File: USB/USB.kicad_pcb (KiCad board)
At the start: 4 copper layers, 36.9 x 37.9 mm, 41 parts, among them J1 MISC1, U1 TLV61222

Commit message: Update
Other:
- board text added: "PCB3D_BR_USB"
- board text added: "PCB3D_TL_USB"

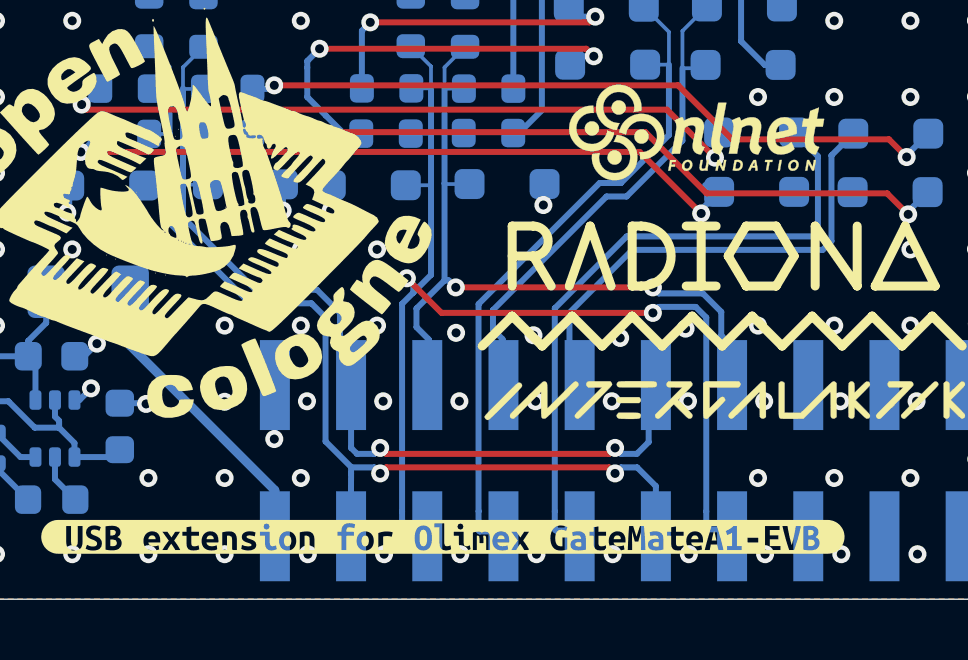
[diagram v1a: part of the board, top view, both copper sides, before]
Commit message: Updating USB
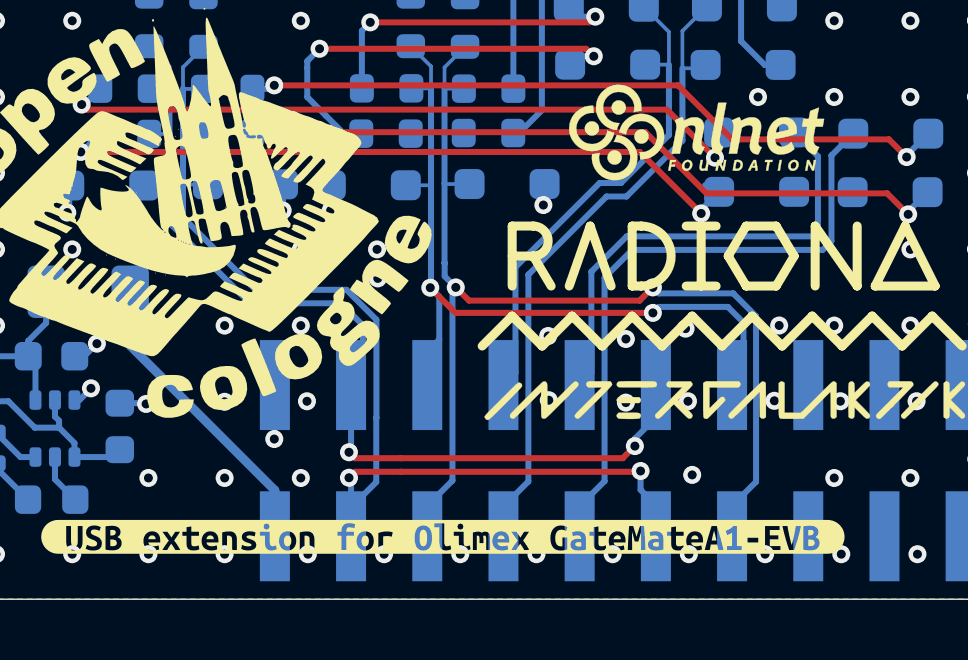
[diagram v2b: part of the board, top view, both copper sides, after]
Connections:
- J1 pad 10: USB1_FPGA_PULL_D+ -> USB1_FPGA_PULL_D-
- J1 pad 11: USB1_FPGA_D- -> USB1_FPGA_D+
- J1 pad 12: USB1_FPGA_D+ -> USB1_FPGA_D-
- J1 pad 13: USB2_FPGA_D- -> USB2_FPGA_D+
- J1 pad 14: USB2_FPGA_D+ -> USB2_FPGA_D-
- J1 pad 15: GN00 -> GP00
- J1 pad 16: GP00 -> GN00
- J1 pad 17: GN01 -> GP01
- J1 pad 18: GP01 -> GN01
- J1 pad 19: GN02 -> GP02
- J1 pad 20: GP02 -> GN02
- J1 pad 3: USB1_FPGA_D- -> USB1_FPGA_D+
- J1 pad 4: USB1_FPGA_D+ -> USB1_FPGA_D-
- J1 pad 5: USB2_FPGA_D- -> USB2_FPGA_D+
- J1 pad 6: USB2_FPGA_D+ -> USB2_FPGA_D-
- J1 pad 7: USB2_FPGA_PULL_D- -> USB2_FPGA_PULL_D+
- J1 pad 8: USB2_FPGA_PULL_D+ -> USB2_FPGA_PULL_D-
- J1 pad 9: USB1_FPGA_PULL_D- -> USB1_FPGA_PULL_D+
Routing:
- net USB2_FPGA_D-: track 39.1 -> 27.4 mm
- net USB2_FPGA_D+: track 26.5 -> 37.7 mm
- net USB2_FPGA_PULL_D-: track 22.5 -> 16.5 mm
- net USB1_FPGA_PULL_D-: track 22.6 -> 16.6 mm
- net USB1_FPGA_D+: track 31.8 -> 37.8 mm
- net USB1_FPGA_PULL_D+: track 16.9 -> 21.7 mm
- net USB2_FPGA_PULL_D+: track 16.9 -> 21.7 mm
- net USB1_FPGA_D-: track 35.0 -> 34.0 mm
- net GND: vias 151 -> 148

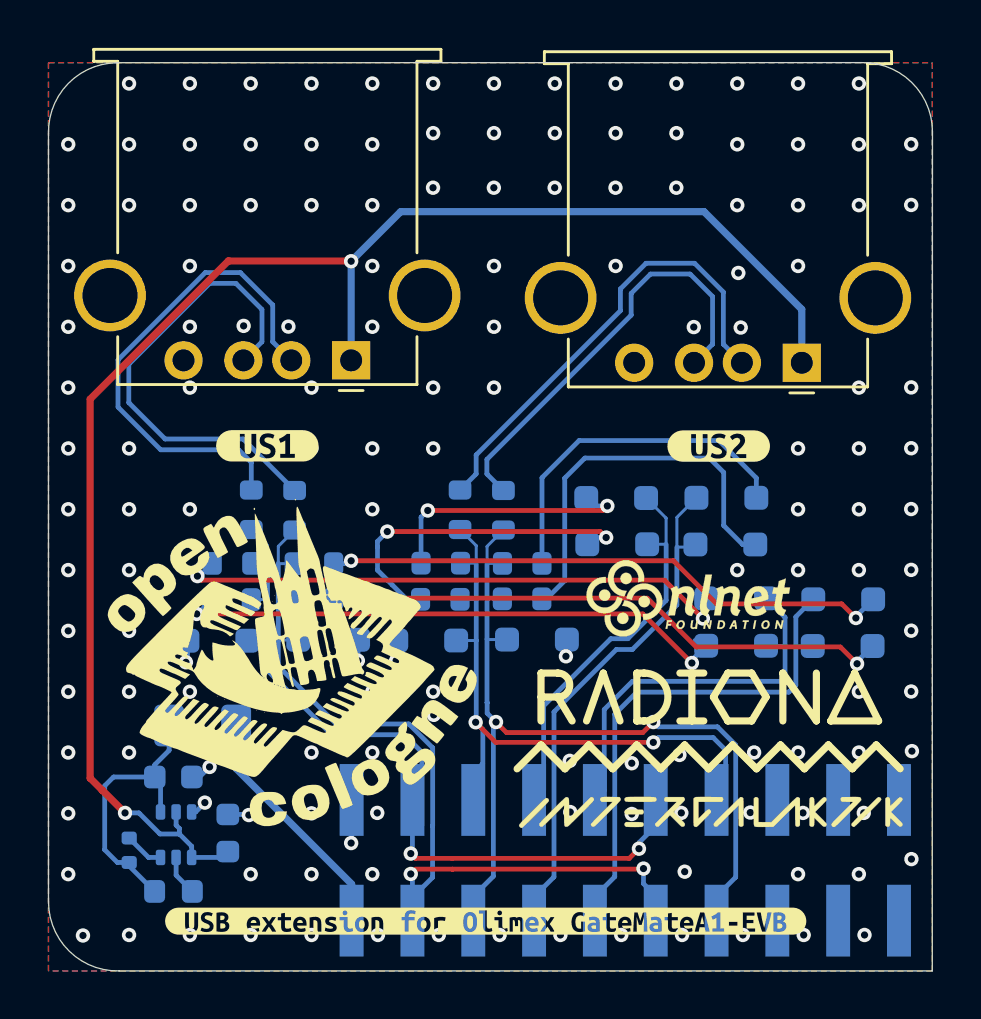
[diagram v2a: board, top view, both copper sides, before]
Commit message: Adding voltage level converter for USB
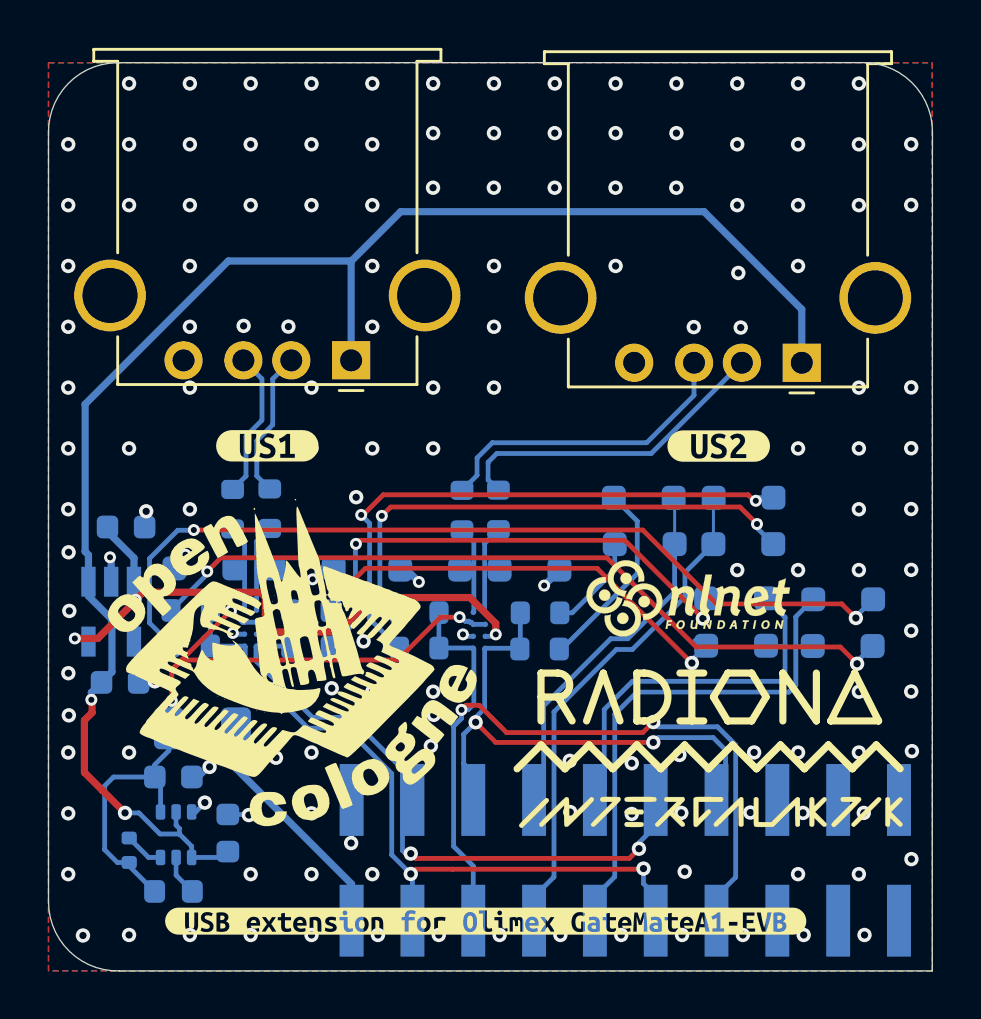
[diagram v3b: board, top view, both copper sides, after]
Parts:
- added C3: 1u, Capacitor_SMD:C_0603_1608Metric, B.Cu at (87.1, 110.0)
- added C4: 1u, Capacitor_SMD:C_0603_1608Metric, B.Cu at (87.3, 103.5)
- added IC1: TXS0202YZPR, TXS0202YZPR:BGA8C50P2X4_89X189X50, B.Cu at (92.5, 107.7)
- added IC2: NCV8730ASN330T1G, NCV8730ASN330T1G:SOT95P275X110-5N, B.Cu at (86.7, 107.0)
- added IC3: TXS0202YZPR, TXS0202YZPR:BGA8C50P2X4_89X189X50, B.Cu at (102.1, 107.8)
- moved R2 6.19 mm to (90.0, 108.4), turned to 0 degrees
- moved D5 5.97 mm to (90.6, 105.2), turned to 180 degrees
- moved R8 5.57 mm to (99.6, 108.5), turned to 0 degrees
- moved R10 5.47 mm to (104.6, 108.6), turned to 180 degrees
- moved D12 5.33 mm to (100.0, 105.3), turned to 180 degrees
- moved D14 5.23 mm to (104.2, 105.3), turned to 0 degrees
- moved R1 5.16 mm to (90.0, 107.0), turned to 0 degrees
- moved R4 4.79 mm to (95.0, 108.5), turned to 180 degrees
- moved D7 4.70 mm to (94.7, 105.2), turned to 0 degrees
- moved R7 4.33 mm to (99.6, 107.1), turned to 0 degrees
- moved R9 4.20 mm to (104.6, 107.1), turned to 0 degrees
- moved R3 3.33 mm to (95.0, 107.0), turned to 0 degrees
- moved R6 2.59 mm to (91.8, 102.7)
- moved R12 1.73 mm to (101.3, 102.8)
- moved R11 1.60 mm to (102.9, 102.8)
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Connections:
- D12 pad 1: USB2_FPGA_D+ -> /USB2_DEVICE_D+
- D14 pad 1: USB2_FPGA_D- -> /USB2_DEVICE_D-
- D5 pad 1: USB1_FPGA_D+ -> /USB1_DEVICE_D+
- D7 pad 1: USB1_FPGA_D- -> /USB1_DEVICE_D-
- R11 pad 1: USB2_FPGA_D- -> /USB2_DEVICE_D-
- R12 pad 1: USB2_FPGA_D+ -> /USB2_DEVICE_D+
- R5 pad 1: USB1_FPGA_D- -> /USB1_DEVICE_D-
- R6 pad 1: USB1_FPGA_D+ -> /USB1_DEVICE_D+
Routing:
- net +3V3: track 0.00 -> 26.5 mm, vias 0 -> 4
- net +2V5: track 11.8 -> 33.0 mm, vias 0 -> 3
- net /FPD1-: track 20.8 -> 6.19 mm
- net /FPD1+: track 19.9 -> 6.22 mm
- net Net-(D2-A): track 23.9 -> 36.6 mm
- net Net-(D10-K): track 14.2 -> 4.12 mm, vias 2 -> 0
- net Net-(D9-A): track 14.6 -> 24.0 mm, vias 0 -> 2
- net Net-(D1-K): track 24.0 -> 32.5 mm
- net USB1_FPGA_D+: track 37.8 -> 30.6 mm
- net USB1_FPGA_D-: track 34.0 -> 27.8 mm
- net /FPD2-: track 19.7 -> 13.7 mm
- net /FPD2+: track 18.2 -> 13.1 mm
- net Net-(D8-K): track 16.7 -> 21.7 mm, vias 0 -> 2
- net Net-(D3-K): track 23.6 -> 18.9 mm
- net /USB1_DEVICE_D-: track 0.00 -> 4.36 mm
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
